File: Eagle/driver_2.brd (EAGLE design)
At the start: 100.3 x 156.2 mm, 21 parts, among them CON1 V6, CON4 V2, CON5 V1, CON6 VA, CON7 VB, CON8 V3, IC1 74HC688N, IC4 74HC688N, IC5 74HC32N

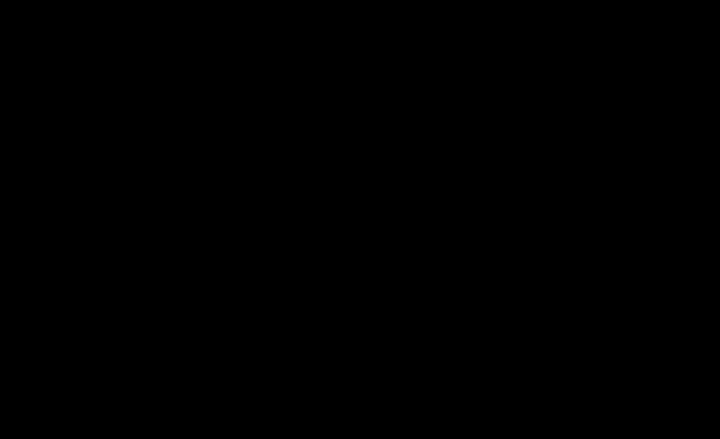
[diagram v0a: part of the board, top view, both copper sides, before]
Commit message: Bug fix
Fogrot to add a diode to /HALT Signal... very bad :-(
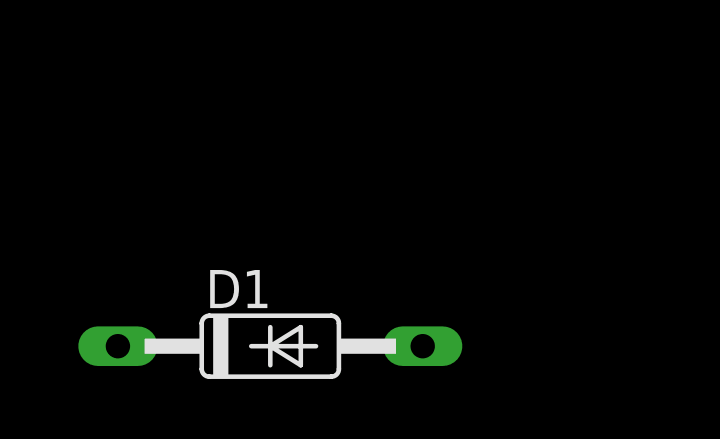
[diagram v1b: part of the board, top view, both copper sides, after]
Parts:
- added D1: BAT42, diode:DO35-10
- IC2, IC3: value (none) -> 27C256
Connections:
- new net N$5: D1.A, TP1.TP
- net /HOLD: now also D1.C; no longer TP1.TP
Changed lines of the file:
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@@
 <layer number="97" name="Info" color="7" fill="1" visible="no" active="no"/>
 <layer number="98" name="Guide" color="6" fill="1" visible="no" active="no"/>
+<layer number="99" name="SpiceOrder" color="5" fill="1" visible="no" active="no"/>
 </layers>
 <board>
@@
 <attribute name="MF" value="" x="218.948" y="27.686" size="1.778" layer="27" rot="R90" display="off"/>
 </element>
-<element name="IC2" library="memory-hitachi" package="DIL28-6" value="" x="71.12" y="81.28" rot="R90">
+<element name="IC2" library="memory-hitachi" package="DIL28-6" value="27C256" x="71.12" y="81.28" rot="R90">
 <attribute name="MPN" value="" x="269.24" y="43.18" size="1.778" layer="27" rot="R90" display="off"/>
 <attribute name="OC_FARNELL" value="unknown" x="269.24" y="43.18" size="1.778" layer="27" rot="R90" display="off"/>
@@
 <attribute name="MF" value="" x="269.24" y="43.18" size="1.778" layer="27" rot="R90" display="off"/>
 </element>
-<element name="IC3" library="memory-hitachi" package="DIL28-6" value="" x="34.29" y="45.72" rot="R90">
+<element name="IC3" library="memory-hitachi" package="DIL28-6" value="27C256" x="34.29" y="45.72" rot="R90">
 <attribute name="MPN" value="" x="232.41" y="45.72" size="1.778" layer="27" rot="R90" display="off"/>
 <attribute name="OC_FARNELL" value="unknown" x="232.41" y="45.72" size="1.778" layer="27" rot="R90" display="off"/>
@@
 </element>
 <element name="R1" library="rcl" package="0204/5" value="4k7" x="87.63" y="90.17" rot="R270"/>
+<element name="D1" library="diode" package="DO35-10" value="BAT42" x="-41.91" y="-6.35"/>
 </elements>
 <signals>
@@
 <contactref element="SV4" pad="2"/>
 <contactref element="IC5" pad="3"/>
+<contactref element="D1" pad="C"/>
+<wire x1="-45.72" y1="68.58" x2="90.17" y2="120.65" width="0" layer="19" extent="1-1"/>
+<wire x1="-46.99" y1="-6.35" x2="-45.72" y2="68.58" width="0" layer="19" extent="1-1"/>
+</signal>
+<signal name="N$5">
+<contactref element="D1" pad="A"/>
 <contactref element="TP1" pad="TP"/>
-<wire x1="95.25" y1="80.01" x2="90.17" y2="120.65" width="0" layer="19" extent="1-1"/>
-<wire x1="-45.72" y1="68.58" x2="95.25" y2="80.01" width="0" layer="19" extent="1-1"/>
+<wire x1="-36.83" y1="-6.35" x2="95.25" y2="80.01" width="0" layer="19" extent="1-1"/>
 </signal>
 </signals>
